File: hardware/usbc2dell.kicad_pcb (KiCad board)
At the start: 2 copper layers, 39.5 x 26.5 mm, 22 parts, among them J1 USB_C_Receptacle_PowerOnly_6P, J2 DELL_Charger, Q1 Q_NMOS_GDS, Q2 Q_NPN_BEC, SW1 SW_DIP_x04, U1 ATtiny1616-M, U2 FUSB302BMPX, U3 L7805

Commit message: improve silkscreen
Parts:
- added REF**: KiCad-Logo2_5mm_SilkScreen, Symbol:KiCad-Logo2_5mm_SilkScreen, B.Cu at (104.7, 68.3)
- added REF**: OSHW-Logo_5.7x6mm_SilkScreen, Symbol:OSHW-Logo_5.7x6mm_SilkScreen, B.Cu at (92.6, 80.8)
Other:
- board text added: "/ ziptie \ \ here /"
- board text added: "@h3wastooshort /usbc2dell"

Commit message: add caps
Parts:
- added C1: 100n, Capacitor_SMD:C_0603_1608Metric, F.Cu at (96.6, 68.1)
- added C2: 1u, Capacitor_SMD:C_0603_1608Metric, F.Cu at (98.1, 68.1)
- added C3: 100n, Capacitor_SMD:C_0603_1608Metric, F.Cu at (105.1, 78.5)
- added C4: 1u, Capacitor_SMD:C_0603_1608Metric, F.Cu at (102.0, 78.5)
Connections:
- net Net-(J2-Pin_3) renamed /Vout
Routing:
- net VCC: track 34.9 -> 37.2 mm
- net /ID_PIN: track 14.4 -> 15.9 mm
- net /PWR_EN: track 11.6 -> 12.3 mm
- added copper zone on F.Cu, net /Vout
- added copper zone on F.Cu, net VCC

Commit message: DRC
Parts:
- moved SW1 0.27 mm to (89.0, 73.2)
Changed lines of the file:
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@@
 			)
 		)
-		(attr board_only exclude_from_pos_files exclude_from_bom)
+		(attr board_only exclude_from_pos_files exclude_from_bom allow_missing_courtyard)
 		(fp_circle
 			(center 0 0)
@@
 			)
 		)
-		(attr board_only exclude_from_pos_files exclude_from_bom)
+		(attr board_only exclude_from_pos_files exclude_from_bom allow_missing_courtyard)
 		(fp_circle
 			(center 0 0)
@@
 	(footprint "Button_Switch_THT:SW_DIP_SPSTx04_Slide_9.78x12.34mm_W7.62mm_P2.54mm"
 		(layer "F.Cu")
-		(at 88.7325 73.2025)
+		(at 89 73.2)
 		(descr "4x-dip-switch SPST , Slide, row spacing 7.62 mm (300 mils), body size 9.78x12.34mm (see e.g. https://www.ctscorp.com/wp-content/uploads/206-208.pdf)")
 		(tags "DIP Switch SPST Slide 7.62mm 300mil")
@@
 		(sheetname "/")
 		(sheetfile "usbc2dell.kicad_sch")
-		(attr through_hole)
+		(attr through_hole allow_missing_courtyard)
 		(fp_line
 			(start 13.92 -5.12)

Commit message: more GND vias
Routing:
- net GND: vias 45 -> 59
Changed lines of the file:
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@@
 	(via
 		(at 104.14 81.64)
+		(size 0.8)
+		(drill 0.4)
+		(layers "F.Cu" "B.Cu")
+		(net 8)
+	)
+	(via
+		(at 89.5 66.5)
+		(size 0.8)
+		(drill 0.4)
+		(layers "F.Cu" "B.Cu")
+		(free yes)
+		(net 8)
+	)
+	(via
+		(at 89.5 65.5)
+		(size 0.8)
+		(drill 0.4)
+		(layers "F.Cu" "B.Cu")
+		(free yes)
+		(net 8)
+	)
+	(via
+		(at 106 75)
+		(size 0.8)
+		(drill 0.4)
+		(layers "F.Cu" "B.Cu")
+		(free yes)
+		(net 8)
+	)
+	(via
+		(at 118.1 71.5)
+		(size 0.8)
+		(drill 0.4)
+		(layers "F.Cu" "B.Cu")
+		(free yes)
+		(net 8)
+	)
+	(via
+		(at 106 72)
+		(size 0.8)
+		(drill 0.4)
+		(layers "F.Cu" "B.Cu")
+		(free yes)
+		(net 8)
+	)
+	(via
+		(at 118.1 75.5)
+		(size 0.8)
+		(drill 0.4)
+		(layers "F.Cu" "B.Cu")
+		(free yes)
+		(net 8)
+	)
+	(via
+		(at 106 76)
+		(size 0.8)
+		(drill 0.4)
+		(layers "F.Cu" "B.Cu")
+		(free yes)
+		(net 8)
+	)
+	(via
+		(at 116.5 71.5)
+		(size 0.8)
+		(drill 0.4)
+		(layers "F.Cu" "B.Cu")
+		(free yes)
+		(net 8)
+	)
+	(via
+		(at 115.7 75.5)
+		(size 0.8)
+		(drill 0.4)
+		(layers "F.Cu" "B.Cu")
+		(free yes)
+		(net 8)
+	)
+	(via
+		(at 109 76)
+		(size 0.8)
+		(drill 0.4)
+		(layers "F.Cu" "B.Cu")
+		(free yes)
+		(net 8)
+	)
+	(via
+		(at 106 73)
+		(size 0.8)
+		(drill 0.4)
+		(layers "F.Cu" "B.Cu")
+		(free yes)
+		(net 8)
+	)
+	(via
+		(at 108 76)
+		(size 0.8)
+		(drill 0.4)
+		(layers "F.Cu" "B.Cu")
+		(free yes)
+		(net 8)
+	)
+	(via
+		(at 107.4 81.8)
 		(size 0.6)
 		(drill 0.3)
 		(layers "F.Cu" "B.Cu")
-		(net 8)
-	)
-	(via
-		(at 89.5 66.5)
-		(size 0.8)
-		(drill 0.4)
-		(layers "F.Cu" "B.Cu")
-		(free yes)
-		(net 8)
-	)
-	(via
-		(at 89.5 65.5)
-		(size 0.8)
-		(drill 0.4)
-		(layers "F.Cu" "B.Cu")
-		(free yes)
-		(net 8)
-	)
-	(via
-		(at 106 75)
-		(size 0.8)
-		(drill 0.4)
-		(layers "F.Cu" "B.Cu")
-		(free yes)
-		(net 8)
-	)
-	(via
-		(at 106 72)
-		(size 0.8)
-		(drill 0.4)
-		(layers "F.Cu" "B.Cu")
-		(free yes)
-		(net 8)
-	)
-	(via
-		(at 106 76)
-		(size 0.8)
-		(drill 0.4)
-		(layers "F.Cu" "B.Cu")
-		(free yes)
-		(net 8)
-	)
-	(via
-		(at 109 76)
-		(size 0.8)
-		(drill 0.4)
-		(layers "F.Cu" "B.Cu")
-		(free yes)
-		(net 8)
-	)
-	(via
-		(at 106 73)
-		(size 0.8)
-		(drill 0.4)
-		(layers "F.Cu" "B.Cu")
-		(free yes)
-		(net 8)
-	)
-	(via
-		(at 108 76)
-		(size 0.8)
-		(drill 0.4)
-		(layers "F.Cu" "B.Cu")
 		(free yes)
 		(net 8)
@@
 	)
 	(via
+		(at 106.8 81.8)
+		(size 0.6)
+		(drill 0.3)
+		(layers "F.Cu" "B.Cu")
+		(free yes)
+		(net 8)
+	)
+	(via
+		(at 117.3 75.5)
+		(size 0.8)
+		(drill 0.4)
+		(layers "F.Cu" "B.Cu")
+		(free yes)
+		(net 8)
+	)
+	(via
 		(at 89.5 64.5)
 		(size 0.8)
@@
 	)
 	(via
+		(at 114.9 71.5)
+		(size 0.8)
+		(drill 0.4)
+		(layers "F.Cu" "B.Cu")
+		(free yes)
+		(net 8)
+	)
+	(via
 		(at 105 73)
 		(size 0.8)
@@
 	)
 	(via
+		(at 97.3 82.8)
+		(size 0.6)
+		(drill 0.3)
+		(layers "F.Cu" "B.Cu")
+		(free yes)
+		(net 8)
+	)
+	(via
+		(at 115.7 71.5)
+		(size 0.8)
+		(drill 0.4)
+		(layers "F.Cu" "B.Cu")
+		(free yes)
+		(net 8)
+	)
+	(via
+		(at 117.3 71.5)
+		(size 0.8)
+		(drill 0.4)
+		(layers "F.Cu" "B.Cu")
+		(free yes)
+		(net 8)
+	)
+	(via
+		(at 116.5 75.5)
+		(size 0.8)
+		(drill 0.4)
+		(layers "F.Cu" "B.Cu")
+		(free yes)
+		(net 8)
+	)
+	(via
 		(at 89.5 67.5)
 		(size 0.8)
@@
 	)
 	(via
+		(at 96.6 82.8)
+		(size 0.6)
+		(drill 0.3)
+		(layers "F.Cu" "B.Cu")
+		(free yes)
+		(net 8)
+	)
+	(via
 		(at 88.5 64.5)
 		(size 0.8)
@@
 		(size 0.8)
 		(drill 0.4)
+		(layers "F.Cu" "B.Cu")
+		(free yes)
+		(net 8)
+	)
+	(via
+		(at 114.9 75.5)
+		(size 0.8)
+		(drill 0.4)

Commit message: silkscreen
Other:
- board text added: ":3"
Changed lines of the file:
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@@
 			(at 0 1.998 0)
 			(layer "B.SilkS")
+			(hide yes)
 			(effects
 				(font
@@
 		)
 		(property "Value" "PROG"
-			(at 0 -2.05 0)
-			(layer "B.Fab")
+			(at 0 1.9 0)
+			(layer "B.SilkS")
 			(effects
 				(font
@@
 			(at 0 1.998 0)
 			(layer "B.SilkS")
+			(hide yes)
 			(effects
 				(font
@@
 		)
 		(property "Value" "RX"
-			(at 0 -2.05 0)
-			(layer "B.Fab")
+			(at 0 1.9 0)
+			(layer "B.SilkS")
 			(effects
 				(font
@@
 			(at 0 1.998 0)
 			(layer "B.SilkS")
+			(hide yes)
 			(effects
 				(font
@@
 		)
 		(property "Value" "TX"
-			(at 0 -2.05 0)
-			(layer "B.Fab")
+			(at 0 1.9 0)
+			(layer "B.SilkS")
 			(effects
 				(font
@@
 		)
 	)
+	(gr_text ":3"
+		(at 93.9 63.9 90)
+		(layer "B.SilkS")
+		(effects
+			(font
+				(face "Liberation Sans")
+				(size 2 2)
+				(thickness 0.1)
+			)
+			(justify left bottom mirror)
+		)
+		(render_cache ":3" 90
+			(polygon
+				(pts
+					(xy 92.364187 64.155478) (xy 92.082819 64.155478) (xy 92.082819 64.421946) (xy 92.364187 64.421946)
+				)
+			)
+			(polygon
+				(pts
+					(xy 93.56 64.155478) (xy 93.278632 64.155478) (xy 93.278632 64.421946) (xy 93.56 64.421946)
+				)
+			)
+			(polygon
+				(pts
+					(xy 93.030115 66.110886) (xy 93.161854 66.099292) (xy 93.272312 66.066538) (xy 93.36556 66.014142)
+					(xy 93.444473 65.941503) (xy 93.505481 65.853665) (xy 93.551236 65.746541) (xy 93.58067 65.616199)
+					(xy 93.591263 65.45778) (xy 93.581955 65.310718) (xy 93.555789 65.186187) (xy 93.514677 65.080644)
+					(xy 93.459494 64.991154) (xy 93.387602 64.914588) (xy 93.300448 64.854747) (xy 93.195548 64.811004)
+					(xy 93.069316 64.784281) (xy 93.046113 65.038415) (xy 93.153883 65.064978) (xy 93.236999 65.107659)
+					(xy 93.300422 65.165589) (xy 93.346942 65.240381) (xy 93.376809 65.335896) (xy 93.387686 65.45778)
+					(xy 93.376329 65.578467) (xy 93.344952 65.673904) (xy 93.295607 65.749528) (xy 93.227387 65.80653)
+					(xy 93.138372 65.842379) (xy 93.022055 65.855408) (xy 92.922818 65.841493) (xy 92.842114 65.801624)
+					(xy 92.775369 65.734508) (xy 92.728911 65.649211) (xy 92.698151 65.535499) (xy 92.686709 65.385362)
+					(xy 92.686709 65.246022) (xy 92.473607 65.246022) (xy 92.473607 65.379867) (xy 92.46249 65.512114)
+					(xy 92.432202 65.614503) (xy 92.385558 65.693475) (xy 92.319895 65.754931) (xy 92.240097 65.791876)
+					(xy 92.141681 65.804849) (xy 92.042457 65.793945) (xy 91.962611 65.763355) (xy 91.897805 65.713991)
+					(xy 91.85024 65.647899) (xy 91.81958 65.560146) (xy 91.80829 65.444103) (xy 91.818352 65.338674)
+					(xy 91.846591 65.252299) (xy 91.891699 65.181053) (xy 91.95331 65.124495) (xy 92.030314 65.085519)
+					(xy 92.126538 65.064305) (xy 92.107365 64.817009) (xy 91.992571 64.84046) (xy 91.894542 64.881009)
+					(xy 91.810494 64.938198) (xy 91.738558 65.013014) (xy 91.682254 65.100208) (xy 91.640998 65.199995)
+					(xy 91.615142 65.314603) (xy 91.606057 65.446789) (xy 91.615708 65.59267) (xy 91.642615 65.713645)
+					(xy 91.684572 65.813923) (xy 91.740635 65.896929) (xy 91.813347 65.966291) (xy 91.898281 66.015898)
+					(xy 91.997871 66.046679) (xy 92.115669 66.057519) (xy 92.23469 66.045237) (xy 92.333172 66.010504)
+					(xy 92.415478 65.954326) (xy 92.481665 65.87885) (xy 92.534142 65.780613) (xy 92.571915 65.654518)
+					(xy 92.577411 65.654518) (xy 92.605653 65.793334) (xy 92.654586 65.903502) (xy 92.722857 65.990596)
+					(xy 92.810552 66.057019) (xy 92.911633 66.097012)
+				)
+			)
+		)
+	)

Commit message: parts sel
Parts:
- D1: value LED_RGB -> TC5050RGBF08-3CJH-AF53A
- J1: value USB_C_Receptacle_PowerOnly_6P -> TYPE-C-31-M-17
- Q1: value Q_NMOS_GDS -> MDD50N03D
- Q2: value Q_NPN_BEC -> MMBT5551
- R1: value 10k -> 4k7
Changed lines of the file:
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@@
 			)
 		)
+		(property "LCSC" "C15849"
+			(at 0 0 270)
+			(unlocked yes)
+			(layer "F.Fab")
+			(hide yes)
+			(effects
+				(font
+					(size 1 1)
+					(thickness 0.15)
+				)
+			)
+		)
 		(property ki_fp_filters "C_*")
 		(sheetname "/")
@@
 			)
 		)
+		(property "LCSC" "C15849"
+			(at 0 0 180)
+			(unlocked yes)
+			(layer "F.Fab")
+			(hide yes)
+			(effects
+				(font
+					(size 1 1)
+					(thickness 0.15)
+				)
+			)
+		)
 		(property ki_fp_filters "C_*")
 		(sheetname "/")
@@
 			)
 		)
-		(property "Value" "USB_C_Receptacle_PowerOnly_6P"
+		(property "Value" "TYPE-C-31-M-17"
 			(at 0 4.75 90)
 			(layer "F.Fab")
@@
 			)
 		)
+		(property "LCSC" "C283540"
+			(at 0 0 270)
+			(unlocked yes)
+			(layer "F.Fab")
+			(hide yes)
+			(effects
+				(font
+					(size 1 1)
+					(thickness 0.15)
+				)
+			)
+		)
 		(property ki_fp_filters "USB*C*Receptacle*")
 		(sheetname "/")
@@
 			)
 		)
-		(property "Value" "Q_NMOS_GDS"
+		(property "Value" "MDD50N03D"
 			(at 0 4.5 0)
 			(layer "F.Fab")
@@
 			)
 		)
+		(property "LCSC" "C5357578"
+			(at 0 0 180)
+			(unlocked yes)
+			(layer "F.Fab")
+			(hide yes)
+			(effects
+				(font
+					(size 1 1)
+					(thickness 0.15)
+				)
+			)
+		)
 		(sheetname "/")
 		(sheetfile "usbc2dell.kicad_sch")
@@
 			)
 		)
+		(property "LCSC" "C22775"
+			(at 0 0 0)
+			(unlocked yes)
+			(layer "F.Fab")
+			(hide yes)
+			(effects
+				(font
+					(size 1 1)
+					(thickness 0.15)
+				)
+			)
+		)
 		(property ki_fp_filters "R_*")
 		(sheetname "/")
@@
 			)
 		)
+		(property "LCSC" "C14663"
+			(at 0 0 0)
+			(unlocked yes)
+			(layer "F.Fab")
+			(hide yes)
+			(effects
+				(font
+					(size 1 1)
+					(thickness 0.15)
+				)
+			)
+		)
 		(property ki_fp_filters "C_*")
 		(sheetname "/")
@@
 			)
 		)
+		(property "LCSC" "C23162"
+			(at 0 0 180)
+			(unlocked yes)
+			(layer "F.Fab")
+			(hide yes)
+			(effects
+				(font
+					(size 1 1)
+					(thickness 0.15)
+				)
+			)
+		)
 		(property ki_fp_filters "R_*")
 		(sheetname "/")
@@
 			)
 		)
-		(property "Value" "10k"
+		(property "Value" "4k7"
 			(at -0.175 1.5 90)
 			(layer "F.Fab")
@@
 			)
 		)
+		(property "LCSC" "C23162"
+			(at 0 0 270)
+			(unlocked yes)
+			(layer "F.Fab")
+			(hide yes)
+			(effects
+				(font
+					(size 1 1)
+					(thickness 0.15)
+				)
+			)
+		)
 		(property ki_fp_filters "R_*")
 		(sheetname "/")
@@
 			)
 		)
+		(property "LCSC" "C23162"
+			(at 0 0 180)
+			(unlocked yes)
+			(layer "F.Fab")
+			(hide yes)
+			(effects
+				(font
+					(size 1 1)
+					(thickness 0.15)
+				)
+			)
+		)
 		(property ki_fp_filters "R_*")
 		(sheetname "/")
@@
 			)
 		)
-		(property "Value" "Q_NPN_BEC"
+		(property "Value" "MMBT5551"
 			(at 0 2.4 0)
 			(layer "F.Fab")
@@
 			)
 		)
+		(property "LCSC" "C2145"
+			(at 0 0 180)
+			(unlocked yes)
+			(layer "F.Fab")
+			(hide yes)
+			(effects
+				(font
+					(size 1 1)
+					(thickness 0.15)
+				)
+			)
+		)
 		(sheetname "/")
 		(sheetfile "usbc2dell.kicad_sch")
@@
 			)
 		)
+		(property "LCSC" "C23162"
+			(at 0 0 180)
+			(unlocked yes)
+			(layer "F.Fab")
+			(hide yes)
+			(effects
+				(font
+					(size 1 1)
+					(thickness 0.15)
+				)
+			)
+		)
 		(property ki_fp_filters "R_*")
 		(sheetname "/")
@@
 			)
 		)
+		(property "LCSC" "C442699"
+			(at 0 0 0)
+			(unlocked yes)
+			(layer "F.Fab")
+			(hide yes)
+			(effects
+				(font
+					(size 1 1)
+					(thickness 0.15)
+				)
+			)
+		)
 		(property ki_fp_filters "WQFN*1EP*2.5x2.5mm*P0.5mm*")
 		(sheetname "/")
@@
 			)
 		)
+		(property "LCSC" "C86206"
+			(at 0 0 0)
+			(unlocked yes)
+			(layer "F.Fab")
+			(hide yes)
+			(effects
+				(font
+					(size 1 1)
+					(thickness 0.15)
+				)
+			)
+		)
 		(property ki_fp_filters "TO?252* TO?263* TO?220*")
 		(sheetname "/")
@@
 			)
 		)
-		(property "Value" "LED_RGB"
+		(property "Value" "TC5050RGBF08-3CJH-AF53A"
 			(at 0 3.3 0)
 			(layer "F.Fab")
@@
 			)
 		)
+		(property "LCSC" "C784540"
+			(at 0 0 180)
+			(unlocked yes)
+			(layer "F.Fab")
+			(hide yes)
+			(effects
+				(font
+					(size 1 1)
+					(thickness 0.15)
+				)
+			)
+		)
 		(property ki_fp_filters "LED* LED_SMD:* LED_THT:*")
 		(sheetname "/")
@@
 			)
 		)
+		(property "LCSC" "C14663"
+			(at 0 0 270)
+			(unlocked yes)
+			(layer "F.Fab")
+			(hide yes)
+			(effects
+				(font
+					(size 1 1)
+					(thickness 0.15)
+				)
+			)
+		)
 		(property ki_fp_filters "C_*")
 		(sheetname "/")
@@
 		(sheetname "/")
 		(sheetfile "usbc2dell.kicad_sch")
-		(attr exclude_from_pos_files)
+		(attr exclude_from_pos_files exclude_from_bom)
 		(fp_circle
 			(center 0 0)
@@
 		(sheetname "/")
 		(sheetfile "usbc2dell.kicad_sch")
-		(attr exclude_from_pos_files)
+		(attr exclude_from_pos_files exclude_from_bom)
 		(fp_circle
 			(center 0 0)
@@
 		(sheetname "/")
 		(sheetfile "usbc2dell.kicad_sch")
-		(attr exclude_from_pos_files)
+		(attr exclude_from_pos_files exclude_from_bom)
 		(fp_circle
 			(center 0 0)

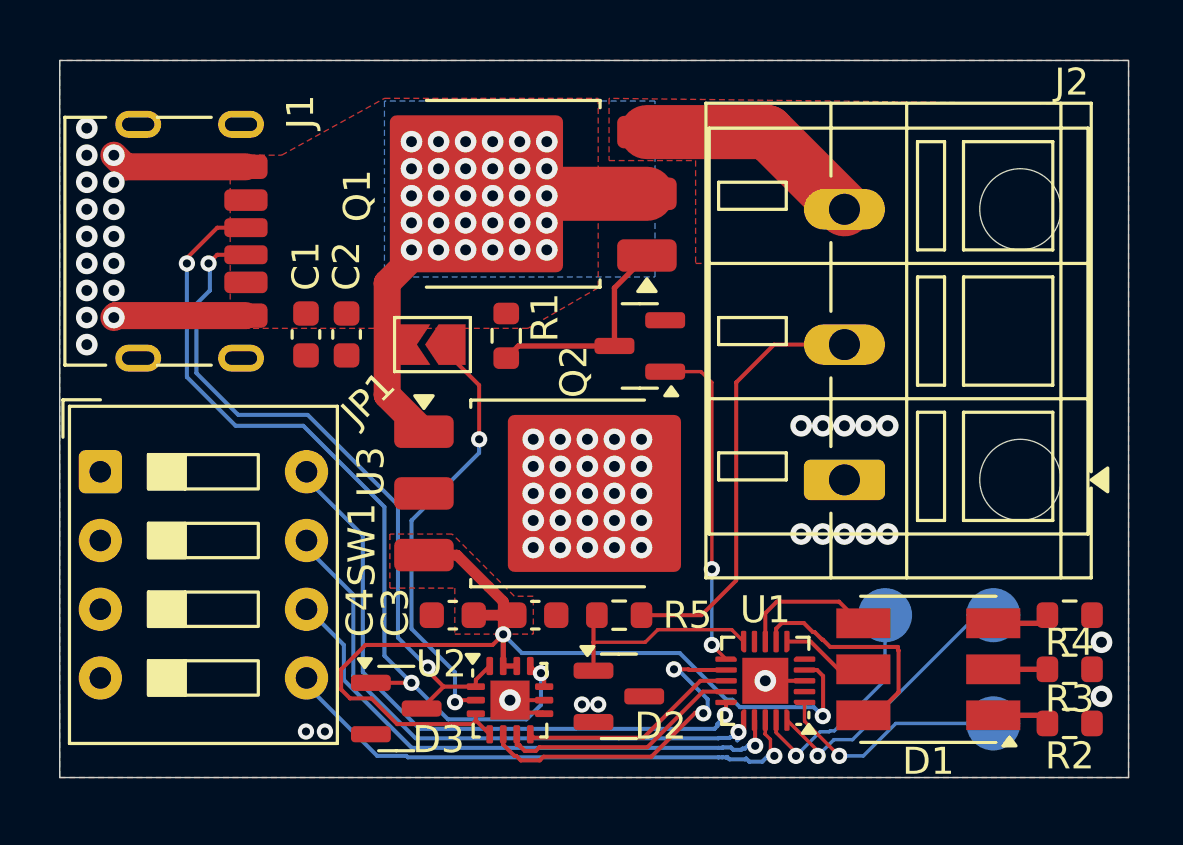
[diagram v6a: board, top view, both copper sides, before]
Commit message: change ESD diodes
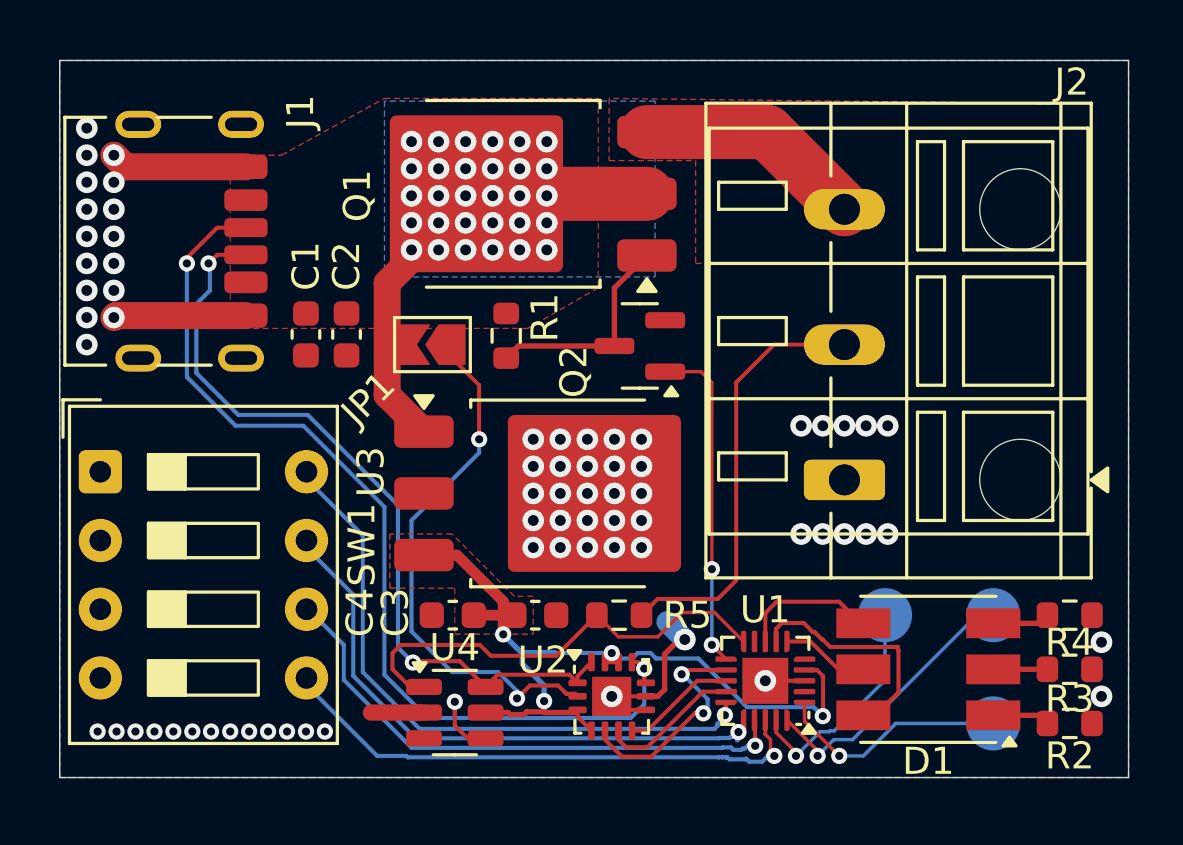
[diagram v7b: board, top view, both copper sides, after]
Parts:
- removed D2, D3: 5V1, Package_TO_SOT_SMD:SOT-23
- added U4: SRV05-4, Package_TO_SOT_SMD:SOT-23-6, F.Cu at (102.1, 82.1)
- moved U2 3.76 mm to (107.9, 81.5)
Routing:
- net /ID: track 8.03 -> 17.1 mm
- net GND: track 14.1 -> 20.1 mm, vias 59 -> 69
- net /CC1: track 32.5 -> 38.2 mm
- net VCC: track 37.2 -> 31.4 mm, vias 2 -> 4
- net /FUSB_INT: track 13.0 -> 8.55 mm
- net /SDA: track 8.16 -> 4.24 mm
- net /SCL: track 9.14 -> 5.28 mm
- net Net-(JP1-A): track 16.1 -> 19.7 mm
- net /CC2: track 26.0 -> 29.1 mm

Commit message: silk
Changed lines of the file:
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@@
 		(tags "capacitor")
 		(property "Reference" "C4"
-			(at 3.425 0.1 90)
+			(at 0.025 -1.3 180)
 			(layer "F.SilkS")
 			(effects
@@
 		(tags "capacitor")
 		(property "Reference" "C3"
-			(at -5.175 -0.1 90)
+			(at -0.075 1.4 180)
 			(layer "F.SilkS")
 			(effects
@@
 		(tags "WQFN NoLead")
 		(property "Reference" "U2"
-			(at -2.54 -1.34 0)
+			(at -2.4 0.5 90)
 			(layer "F.SilkS")
 			(effects
@@
 		(tags "DIP Switch SPST Slide 7.62mm 300mil")
 		(property "Reference" "SW1"
-			(at 9.6675 2.6975 90)
+			(at 9.7 3.7 90)
 			(layer "F.SilkS")
 			(effects
@@
 		(tags "DPAK TO-252 DPAK-3 TO-252-3 SOT-428")
 		(property "Reference" "U3"
-			(at -7 -0.8 90)
+			(at -7 0 90)
 			(layer "F.SilkS")
 			(effects
@@
 			)
 		)
-		(property "LCSC" "C86206"
+		(property "LCSC" " C54285"
 			(at 0 0 0)
 			(unlocked yes)
@@
 		(tags "SOT TO_SOT_SMD")
 		(property "Reference" "U4"
-			(at 0 -2.4 0)
+			(at -2.7 0 90)
 			(layer "F.SilkS")
 			(effects
